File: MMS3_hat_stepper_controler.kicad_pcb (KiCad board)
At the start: 4 copper layers, 100 x 50 mm, 91 parts, among them J1 Chainbus in, J2 Chainbus Out, J3 Conn_01x04_Pin, J4 AMASS XT60 Male, J5 AMASS XT60 Female, J6 Encoder connector, J7 Motor connector, J8 Conn_01x03_Pin, SW1 SW_DIP_x04, U1 SN74CB3Q3384APW, U2 M24C64, U3 TMC5130A-TA, U4 AMS1117, U5 LM2596HVS-ADJRG

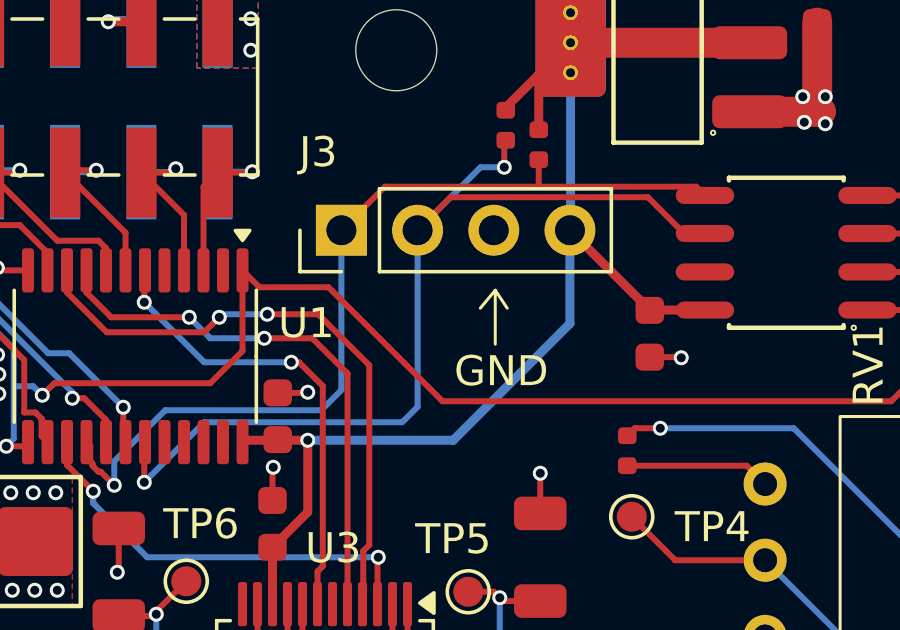
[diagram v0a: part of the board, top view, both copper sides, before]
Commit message: added pullup on select
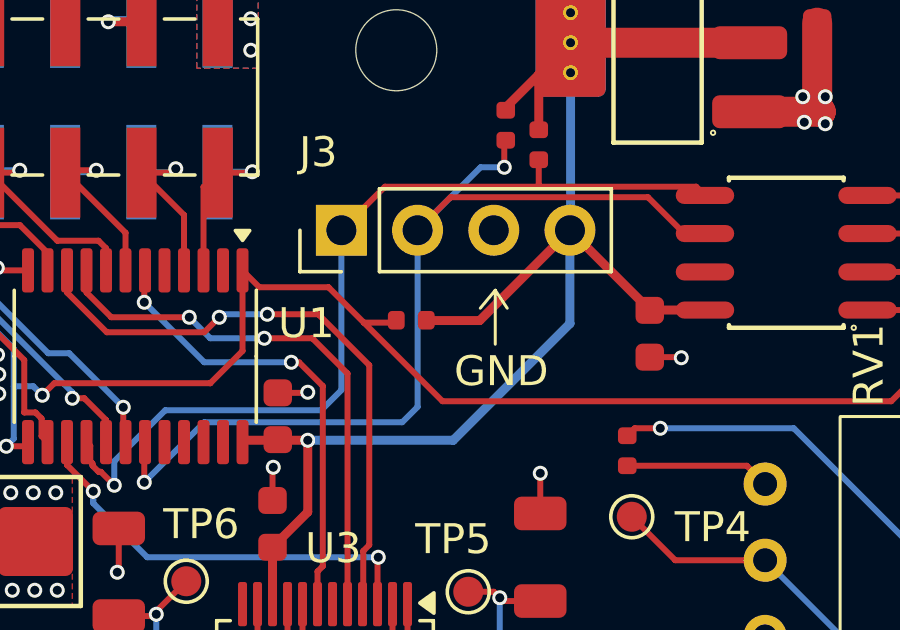
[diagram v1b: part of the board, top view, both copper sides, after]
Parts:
- added R19: 10kΩ, PCM_JLCPCB:R_0402, F.Cu at (153.5, 103.0)
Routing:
- net +3V3: track 46.9 -> 52.9 mm
- net /Bus_switch/SEL1: track 82.6 -> 83.7 mm

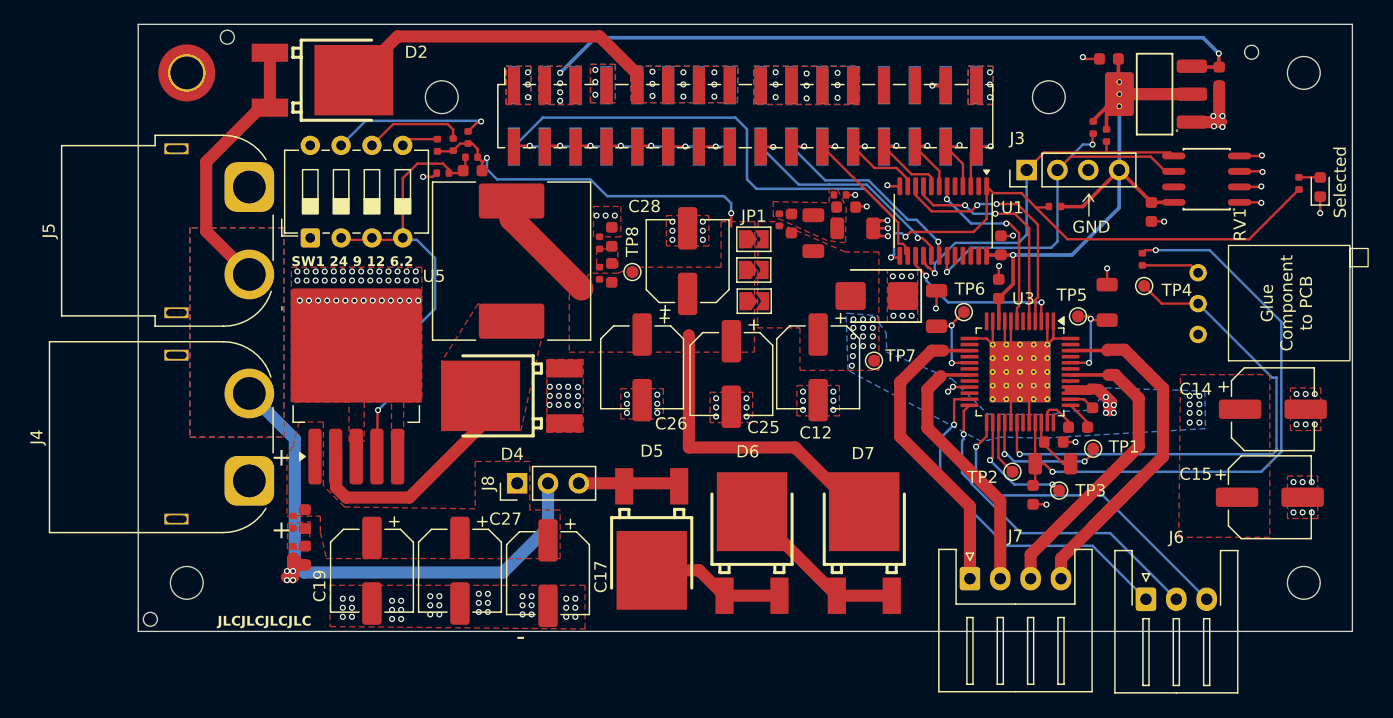
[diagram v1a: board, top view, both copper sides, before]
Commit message: added pinout on silkscreen
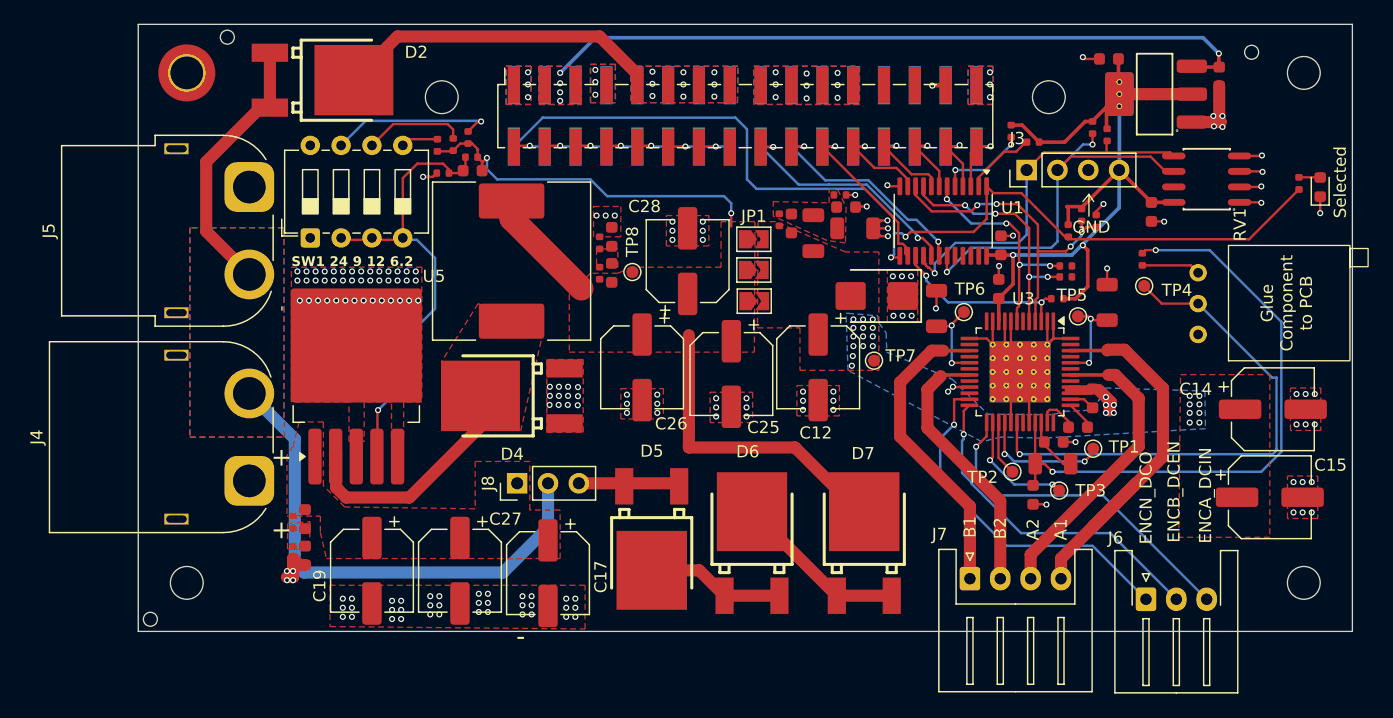
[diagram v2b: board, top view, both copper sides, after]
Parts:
- removed PN1: ~, PCM_JLCPCB:Part_Num_JLCPCB
- added R20: 10kΩ, PCM_JLCPCB:R_0402, F.Cu at (149.9, 96.8)
- added R21: 10kΩ, PCM_JLCPCB:R_0402, F.Cu at (151.7, 97.7)
- added R22: 10kΩ, PCM_JLCPCB:R_0402, F.Cu at (154.4, 107.9)
- added R23: 10kΩ, PCM_JLCPCB:R_0402, F.Cu at (157.8, 97.1)
- added R24: 10kΩ, PCM_JLCPCB:R_0402, F.Cu at (154.4, 108.8)
- added R25: 10kΩ, PCM_JLCPCB:R_0402, F.Cu at (154.6, 105.0)
- added R26: 330Ω, PCM_JLCPCB:R_0402, F.Cu at (173.6, 101.1)
- R1: value 330Ω -> 10kΩ
- moved R1 22.1 mm to (153.7, 110.6), turned to 180 degrees
- moved R2 7.26 mm to (155.7, 103.7)
- moved R19 7.20 mm to (156.6, 96.5), turned to -90 degrees
- moved R3 7.10 mm to (156.9, 104.2), turned to 90 degrees
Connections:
- R1 pad 1: /Bus_switch/SEL1 -> +3V3
- R1 pad 2: Net-(D1-A) -> /Bus_switch/Chainbus.CS
- R19 pad 2: /Bus_switch/SEL1 -> /Bus_switch/Chainbus.SCL
- R2 pad 2: /Bus_switch/Chainbus.SCL -> /Bus_switch/Chainbus.SCK
- R3 pad 1: +3V3 -> /Bus_switch/Chainbus.SCK
- R3 pad 2: /Bus_switch/Chainbus.SDA -> GND
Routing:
- net +3V3: track 52.9 -> 67.9 mm, vias 1 -> 2
- net /Bus_switch/Chainbus.TX: track 0.00 -> 7.22 mm, vias 0 -> 2
- net /Bus_switch/Chainbus.SCK: track 20.4 -> 27.1 mm, vias 2 -> 4
- net /Bus_switch/Chainbus.RX: track 0.00 -> 5.81 mm
- net /Bus_switch/Chainbus.MISO: track 15.5 -> 18.9 mm, vias 2 -> 4
- net /Bus_switch/Chainbus.MOSI: track 18.2 -> 20.8 mm, vias 2 -> 4
- net GND: track 71.6 -> 72.7 mm, vias 181 -> 182
- net /Bus_switch/SEL1: track 83.7 -> 82.6 mm
- net /Bus_switch/Chainbus.CS: track 14.2 -> 15.1 mm
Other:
- board text added: "3"
- board text added: "A1"
- board text added: "A2"
- board text added: "B1"
- board text added: "B2"
- board text added: "ENCA_DCIN"
- board text added: "ENCB_DCEN"
- board text added: "ENCN_DCO"
- board text removed: "2"
